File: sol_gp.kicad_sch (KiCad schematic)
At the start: 21 parts, among them J122 J122 Sol 25-28 drive + tie-ba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, J123 J123 Sol 25-28 drive (backbox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, J124 J124 Sol 25-28 drive (backbox), Q20 IRLR3110ZTRPBF, Q22 IRLR3110ZTRPBF, Q24 IRLR3110ZTRPBF, Q26 IRLR3110ZTRPBF, U2 74HCT574

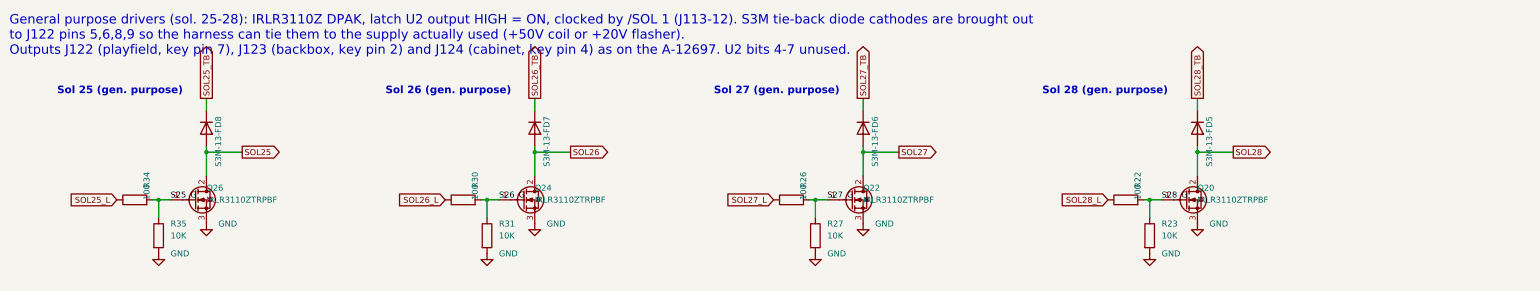
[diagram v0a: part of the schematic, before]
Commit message: Prepare WPC engineering candidate and verification tooling
Include revised PCB and schematics, component models, fabrication exports, renders, BOM, assembly counts, and reproducible electrical and manufacturing checks. Document unresolved replay convergence, regulator fault behavior, and physical qualification gates; this candidate is not production released.
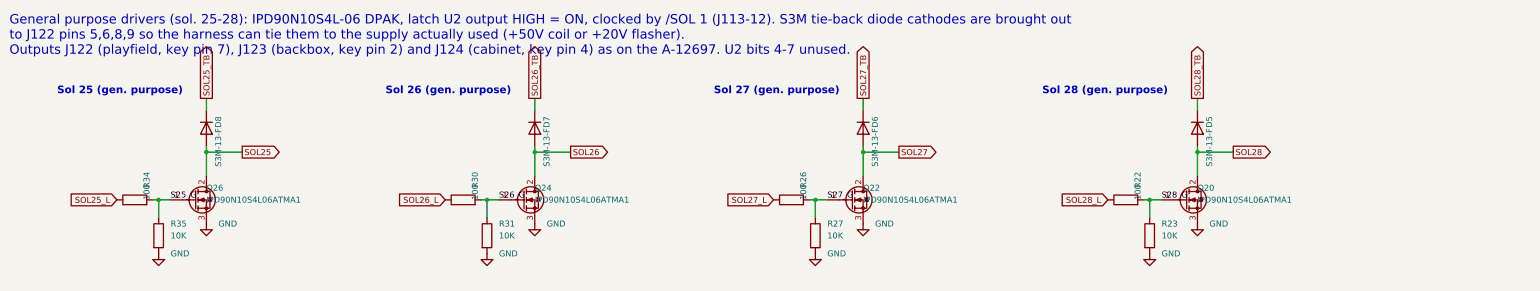
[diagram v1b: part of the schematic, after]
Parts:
- B2: symbol Device:C -> wpc_symbols:Device_C
- D5, D6, D7, D8: symbol Diode:1N4007 -> wpc_symbols:Diode_1N4007
- J122: symbol Connector_Generic:Conn_01x09 -> wpc_symbols:Connector_Generic_Conn_01x09; MPN 0026604009 -> 0026604090
- J123, J124: symbol Connector_Generic:Conn_01x05 -> wpc_symbols:Connector_Generic_Conn_01x05; Link https://www.digikey.com/en/products/result?keywords=0026604005 -> https://www.digikey.com/en/products/result?keywords=0026604050; MPN 0026604005 -> 0026604050
- Q20, Q22, Q24, Q26: value IRLR3110ZTRPBF -> IPD90N10S4L06ATMA1; symbol Transistor_FET:Q_NMOS_GDS -> wpc_symbols:Transistor_FET_Q_NMOS_GDS; Link https://www.digikey.com/en/products/detail/infineon-technol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 -> https://www.infineon.com/part/IPD90N10S4L-06; MPN IRLR3110ZTRPBF -> IPD90N10S4L06ATMA1
- R22, R23, R26, R27, R30, R31, R34, R35: symbol Device:R -> wpc_symbols:Device_R
- U2: symbol 74xx:74HCT574 -> wpc_symbols:74xx_74HCT574
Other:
- note added: "General purpose drivers (sol. 25-28): IPD90N10S4L-06 DPAK, latch U2 output HIGH = ON, clocked by /SOL 1 (J113-12). S3M tie-back diode cathodes are brought out to J122 pins 5,6,8,9 so the harness can tie them to the supply actually used (+50V coil or +20V flasher). Outputs J122 (playfield, key pin 7), J123 (backbox, key pin 2) and J124 (cabinet, key pin 4) as on the A-12697. U2 bits 4-7 unused."
- note removed: "General purpose drivers (sol. 25-28): IRLR3110Z DPAK, latch U2 output HIGH = ON, clocked by /SOL 1 (J113-12). S3M tie-back diode cathodes are brought out to J122 pins 5,6,8,9 so the harness can tie them to the supply actually used (+50V coil or +20V flasher). Outputs J122 (playfield, key pin 7), J123 (backbox, key pin 2) and J124 (cabinet, key pin 4) as on the A-12697. U2 bits 4-7 unused."
- title: Solenoids 25-28 (general purpose, IRLR3110Z) -> Solenoids 25-28 (general purpose, IPD90N10S4L-06)
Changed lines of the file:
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@@
 	(paper "A2")
 	(title_block
-		(title "Solenoids 25-28 (general purpose, IRLR3110Z)")
+		(title "Solenoids 25-28 (general purpose, IPD90N10S4L-06)")
 		(date "2026-09-04")
 		(rev "A")
@@
 		)
 	)
-	(text "General purpose drivers (sol. 25-28): IRLR3110Z DPAK, latch U2 output HIGH = ON, clocked by /SOL 1 (J113-12). S3M tie-back diode cathodes are brought out\nto J122 pins 5,6,8,9 so the harness can tie them to the supply actually used (+50V coil or +20V flasher).\nOutputs J122 (playfield, key pin 7), J123 (backbox, key pin 2) and J124 (cabinet, key pin 4) as on the A-12697. U2 bits 4-7 unused."
+	(text "General purpose drivers (sol. 25-28): IPD90N10S4L-06 DPAK, latch U2 output HIGH = ON, clocked by /SOL 1 (J113-12). S3M tie-back diode cathodes are brought out\nto J122 pins 5,6,8,9 so the harness can tie them to the supply actually used (+50V coil or +20V flasher).\nOutputs J122 (playfield, key pin 7), J123 (backbox, key pin 2) and J124 (cabinet, key pin 4) as on the A-12697. U2 bits 4-7 unused."
 		(exclude_from_sim no)
 		(at 20.32 15.24 0)
@@
 	)
 	(symbol
-		(lib_id "Transistor_FET:Q_NMOS_GDS")
+		(lib_id "wpc_symbols:Transistor_FET_Q_NMOS_GDS")
 		(at 59.69 54.61 0)
 		(unit 1)
@@
 			)
 		)
-		(property "Value" "IRLR3110ZTRPBF"
+		(property "Value" "IPD90N10S4L06ATMA1"
 			(at 62.23 54.61 0)
 			(effects
@@
 			)
 		)
-		(property "Description" "N-MOSFET 100 V 63 A 14 mOhm @10 V / 16 mOhm @4.5 V logic-level, DPAK (TO-252)"
+		(property "Description" "N-MOSFET 100 V, 8.1 mOhm max at 4.5 V, DPAK G-D-S, RthJA 62 C/W minimal footprint; upgraded solenoid driver"
 			(at 59.69 54.61 0)
 			(effects
@@
 			)
 		)
-		(property "MPN" "IRLR3110ZTRPBF"
+		(property "MPN" "IPD90N10S4L06ATMA1"
 			(at 59.69 54.61 0)
 			(effects
@@
 			)
 		)
-		(property "Link" "https://www.digikey.com/en/products/detail/infineon-technologies/IRLR3110ZTRPBF/1928415"
+		(property "Link" "https://www.infineon.com/part/IPD90N10S4L-06"
 			(at 59.69 54.61 0)
 			(effects
@@
 	)
 	(symbol
-		(lib_id "Device:R")
+		(lib_id "wpc_symbols:Device_R")
 		(at 46.99 54.61 90)
 		(unit 1)
@@
 	)
 	(symbol
-		(lib_id "Device:R")
+		(lib_id "wpc_symbols:Device_R")
 		(at 52.07 62.23 0)
 		(unit 1)
@@
 	)
 	(symbol
-		(lib_id "Diode:1N4007")
+		(lib_id "wpc_symbols:Diode_1N4007")
 		(at 62.23 39.37 270)
 		(unit 1)
@@
 	)
 	(symbol
-		(lib_id "power:GND")
+		(lib_id "wpc_symbols:power_GND")
 		(at 52.07 66.04 0)
 		(unit 1)
@@
 	)
 	(symbol
-		(lib_id "power:GND")
+		(lib_id "wpc_symbols:power_GND")
 		(at 62.23 59.69 0)
 		(unit 1)
@@
 	)
 	(symbol
-		(lib_id "Transistor_FET:Q_NMOS_GDS")
+		(lib_id "wpc_symbols:Transistor_FET_Q_NMOS_GDS")
 		(at 129.54 54.61 0)
 		(unit 1)
@@
 			)
 		)
-		(property "Value" "IRLR3110ZTRPBF"
+		(property "Value" "IPD90N10S4L06ATMA1"
 			(at 132.08 54.61 0)
 			(effects
@@
 			)
 		)
-		(property "Description" "N-MOSFET 100 V 63 A 14 mOhm @10 V / 16 mOhm @4.5 V logic-level, DPAK (TO-252)"
+		(property "Description" "N-MOSFET 100 V, 8.1 mOhm max at 4.5 V, DPAK G-D-S, RthJA 62 C/W minimal footprint; upgraded solenoid driver"
 			(at 129.54 54.61 0)
 			(effects
@@
 			)
 		)
-		(property "MPN" "IRLR3110ZTRPBF"
+		(property "MPN" "IPD90N10S4L06ATMA1"
 			(at 129.54 54.61 0)
 			(effects
@@
 			)
 		)
-		(property "Link" "https://www.digikey.com/en/products/detail/infineon-technologies/IRLR3110ZTRPBF/1928415"
+		(property "Link" "https://www.infineon.com/part/IPD90N10S4L-06"
 			(at 129.54 54.61 0)
 			(effects
@@
 	)
 	(symbol
-		(lib_id "Device:R")
+		(lib_id "wpc_symbols:Device_R")
 		(at 116.84 54.61 90)
 		(unit 1)
@@
 	)
 	(symbol
-		(lib_id "Device:R")
+		(lib_id "wpc_symbols:Device_R")
 		(at 121.92 62.23 0)
 		(unit 1)
@@
 	)
 	(symbol
-		(lib_id "Diode:1N4007")
+		(lib_id "wpc_symbols:Diode_1N4007")
 		(at 132.08 39.37 270)
 		(unit 1)
@@
 	)
 	(symbol
-		(lib_id "power:GND")
+		(lib_id "wpc_symbols:power_GND")
 		(at 121.92 66.04 0)
 		(unit 1)
@@
 	)
 	(symbol
-		(lib_id "power:GND")
+		(lib_id "wpc_symbols:power_GND")
 		(at 132.08 59.69 0)
 		(unit 1)
@@
 	)
 	(symbol
-		(lib_id "Transistor_FET:Q_NMOS_GDS")
+		(lib_id "wpc_symbols:Transistor_FET_Q_NMOS_GDS")
 		(at 199.39 54.61 0)
 		(unit 1)
@@
 			)
 		)
-		(property "Value" "IRLR3110ZTRPBF"
+		(property "Value" "IPD90N10S4L06ATMA1"
 			(at 201.93 54.61 0)
 			(effects
@@
 			)
 		)
-		(property "Description" "N-MOSFET 100 V 63 A 14 mOhm @10 V / 16 mOhm @4.5 V logic-level, DPAK (TO-252)"
+		(property "Description" "N-MOSFET 100 V, 8.1 mOhm max at 4.5 V, DPAK G-D-S, RthJA 62 C/W minimal footprint; upgraded solenoid driver"
 			(at 199.39 54.61 0)
 			(effects
@@
 			)
 		)
-		(property "MPN" "IRLR3110ZTRPBF"
+		(property "MPN" "IPD90N10S4L06ATMA1"
 			(at 199.39 54.61 0)
 			(effects
@@
 			)
 		)
-		(property "Link" "https://www.digikey.com/en/products/detail/infineon-technologies/IRLR3110ZTRPBF/1928415"
+		(property "Link" "https://www.infineon.com/part/IPD90N10S4L-06"
 			(at 199.39 54.61 0)
 			(effects
@@
 	)
 	(symbol
-		(lib_id "Device:R")
+		(lib_id "wpc_symbols:Device_R")
 		(at 186.69 54.61 90)
 		(unit 1)
@@
 	)
 	(symbol
-		(lib_id "Device:R")
+		(lib_id "wpc_symbols:Device_R")
 		(at 191.77 62.23 0)
 		(unit 1)
@@
 	)
 	(symbol
-		(lib_id "Diode:1N4007")
+		(lib_id "wpc_symbols:Diode_1N4007")
 		(at 201.93 39.37 270)
 		(unit 1)
@@
 	)
 	(symbol
-		(lib_id "power:GND")
+		(lib_id "wpc_symbols:power_GND")
 		(at 191.77 66.04 0)
 		(unit 1)
@@
 	)
 	(symbol
-		(lib_id "power:GND")
+		(lib_id "wpc_symbols:power_GND")
 		(at 201.93 59.69 0)
 		(unit 1)
@@
 	)
 	(symbol
-		(lib_id "Transistor_FET:Q_NMOS_GDS")
+		(lib_id "wpc_symbols:Transistor_FET_Q_NMOS_GDS")
 		(at 270.51 54.61 0)
 		(unit 1)
@@
 			)
 		)
-		(property "Value" "IRLR3110ZTRPBF"
+		(property "Value" "IPD90N10S4L06ATMA1"
 			(at 273.05 54.61 0)
 			(effects
@@
 			)
 		)
-		(property "Description" "N-MOSFET 100 V 63 A 14 mOhm @10 V / 16 mOhm @4.5 V logic-level, DPAK (TO-252)"
+		(property "Description" "N-MOSFET 100 V, 8.1 mOhm max at 4.5 V, DPAK G-D-S, RthJA 62 C/W minimal footprint; upgraded solenoid driver"
 			(at 270.51 54.61 0)
 			(effects
@@
 			)
 		)
-		(property "MPN" "IRLR3110ZTRPBF"
+		(property "MPN" "IPD90N10S4L06ATMA1"
 			(at 270.51 54.61 0)
 			(effects
@@
 			)
 		)
-		(property "Link" "https://www.digikey.com/en/products/detail/infineon-technologies/IRLR3110ZTRPBF/1928415"
+		(property "Link" "https://www.infineon.com/part/IPD90N10S4L-06"
 			(at 270.51 54.61 0)
 			(effects
@@
 	)
 	(symbol
-		(lib_id "Device:R")
+		(lib_id "wpc_symbols:Device_R")
 		(at 257.81 54.61 90)
 		(unit 1)
@@
 	)
 	(symbol
-		(lib_id "Device:R")
+		(lib_id "wpc_symbols:Device_R")
 		(at 262.89 62.23 0)
 		(unit 1)
@@
 	)
 	(symbol
-		(lib_id "Diode:1N4007")
+		(lib_id "wpc_symbols:Diode_1N4007")
 		(at 273.05 39.37 270)
 		(unit 1)
@@
 	)
 	(symbol
-		(lib_id "power:GND")
+		(lib_id "wpc_symbols:power_GND")
 		(at 262.89 66.04 0)
 		(unit 1)
@@
 	)
 	(symbol
-		(lib_id "power:GND")
+		(lib_id "wpc_symbols:power_GND")
 		(at 273.05 59.69 0)
 		(unit 1)
@@
 	)
 	(symbol
-		(lib_id "74xx:74HCT574")
+		(lib_id "wpc_symbols:74xx_74HCT574")
 		(at 59.69 149.86 0)
 		(unit 1)
@@
 	)
 	(symbol
-		(lib_id "power:+5V")
+		(lib_id "wpc_symbols:power_+5V")
 		(at 59.69 129.54 0)
 		(unit 1)
@@
 	)
 	(symbol
-		(lib_id "power:GND")
+		(lib_id "wpc_symbols:power_GND")
 		(at 59.69 170.18 0)
 		(unit 1)
@@
 	)
 	(symbol
-		(lib_id "Device:C")
+		(lib_id "wpc_symbols:Device_C")
 		(at 110.49 134.62 0)
 		(unit 1)
@@
 	)
 	(symbol
-		(lib_id "power:+5V")
+		(lib_id "wpc_symbols:power_+5V")
 		(at 110.49 130.81 0)
 		(unit 1)
@@
 	)
 	(symbol
-		(lib_id "power:GND")
+		(lib_id "wpc_symbols:power_GND")
 		(at 110.49 138.43 0)
 		(unit 1)
@@
 	)
 	(symbol
-		(lib_id "Connector_Generic:Conn_01x09")
+		(lib_id "wpc_symbols:Connector_Generic_Conn_01x09")
 		(at 299.72 139.7 0)
 		(unit 1)
@@
 			)
 		)
-		(property "MPN" "0026604009"
+		(property "MPN" "0026604090"
 			(at 299.72 139.7 0)
 			(effects
@@
 	)
 	(symbol
-		(lib_id "Connector_Generic:Conn_01x05")
+		(lib_id "wpc_symbols:Connector_Generic_Conn_01x05")
 		(at 359.41 139.7 0)
 		(unit 1)
@@
 			)
 		)
-		(property "MPN" "0026604005"
+		(property "MPN" "0026604050"
 			(at 359.41 139.7 0)
 			(effects
@@
 			)
 		)
-		(property "Link" "https://www.digikey.com/en/products/result?keywords=0026604005"
+		(property "Link" "https://www.digikey.com/en/products/result?keywords=0026604050"
 			(at 359.41 139.7 0)
 			(effects
@@
 	)
 	(symbol
-		(lib_id "Connector_Generic:Conn_01x05")
+		(lib_id "wpc_symbols:Connector_Generic_Conn_01x05")
 		(at 359.41 190.5 0)
 		(unit 1)
@@
 			)
 		)
-		(property "MPN" "0026604005"
+		(property "MPN" "0026604050"
 			(at 359.41 190.5 0)
 			(effects
@@
 			)
 		)
-		(property "Link" "https://www.digikey.com/en/products/result?keywords=0026604005"
+		(property "Link" "https://www.digikey.com/en/products/result?keywords=0026604050"
 			(at 359.41 190.5 0)
 			(effects
